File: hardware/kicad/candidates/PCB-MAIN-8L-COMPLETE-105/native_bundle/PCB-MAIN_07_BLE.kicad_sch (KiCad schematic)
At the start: 11 parts, among them U11 MDBT50Q-P1MV2, U6 Single non-inverting open-dra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

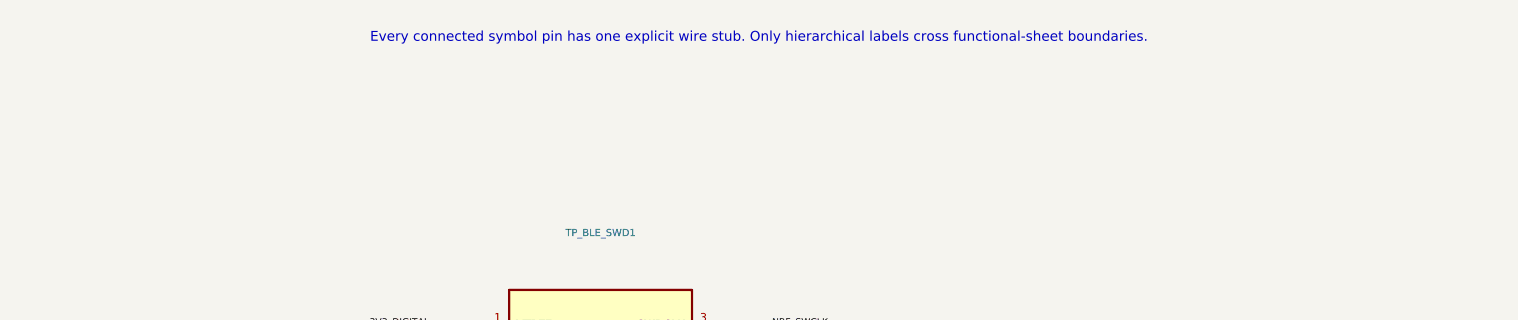
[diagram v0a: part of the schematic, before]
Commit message: PCB-MAIN Rev B: bilingual schematic notes and PDF
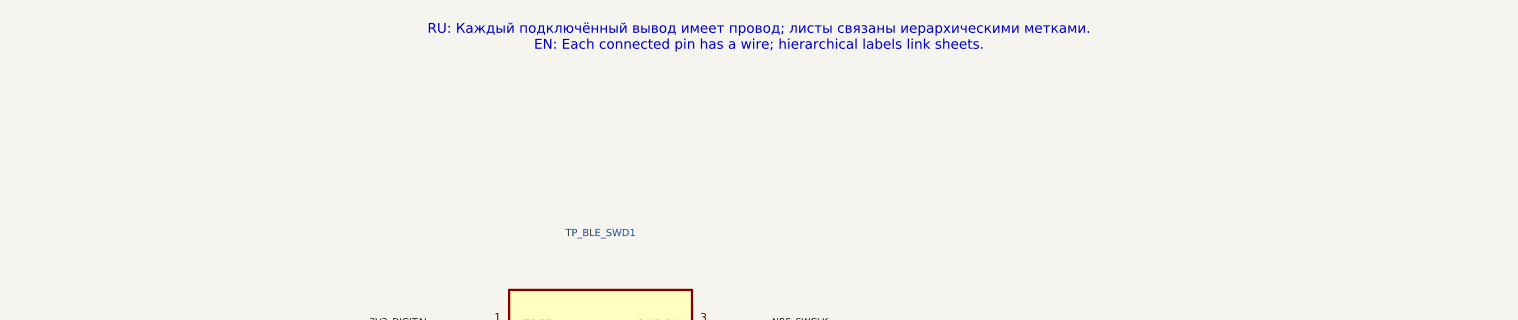
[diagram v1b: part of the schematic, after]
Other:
- note added: "RU: Каждый подключённый вывод имеет провод; листы связаны иерархическими метками. EN: Each connected pin has a wire; hierarchical labels link sheets."
- note removed: "Every connected symbol pin has one explicit wire stub. Only hierarchical labels cross functional-sheet boundaries."
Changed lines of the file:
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@@
     (stroke (width 0.0))
   )
-  (text "Every connected symbol pin has one explicit wire stub. Only hierarchical labels cross functional-sheet boundaries."
+  (text "RU: Каждый подключённый вывод имеет провод; листы связаны иерархическими метками.\nEN: Each connected pin has a wire; hierarchical labels link sheets."
     (at 297.0 12.7 0)
     (effects (font (size 1.1 1.1)))
